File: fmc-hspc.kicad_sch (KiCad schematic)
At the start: 36 parts, among them J12 ASP-184329-01_mounting_holes_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

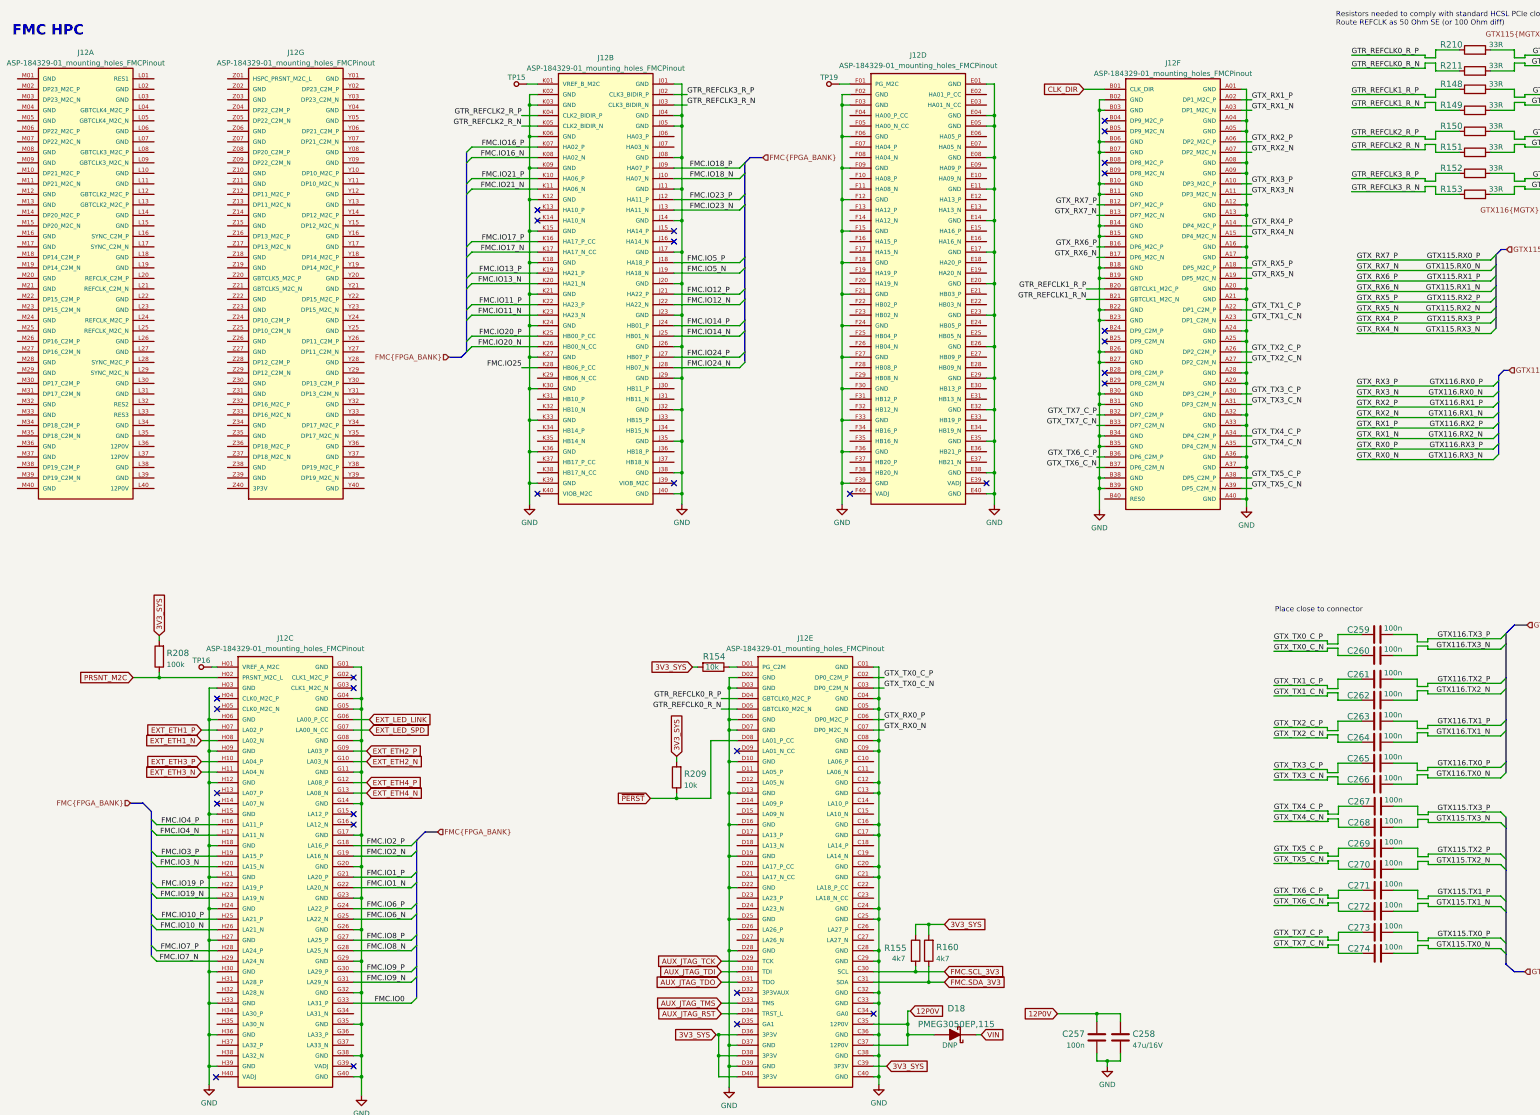
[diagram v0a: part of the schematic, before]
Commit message: Re-annotate the schematic. Export changes to PCB
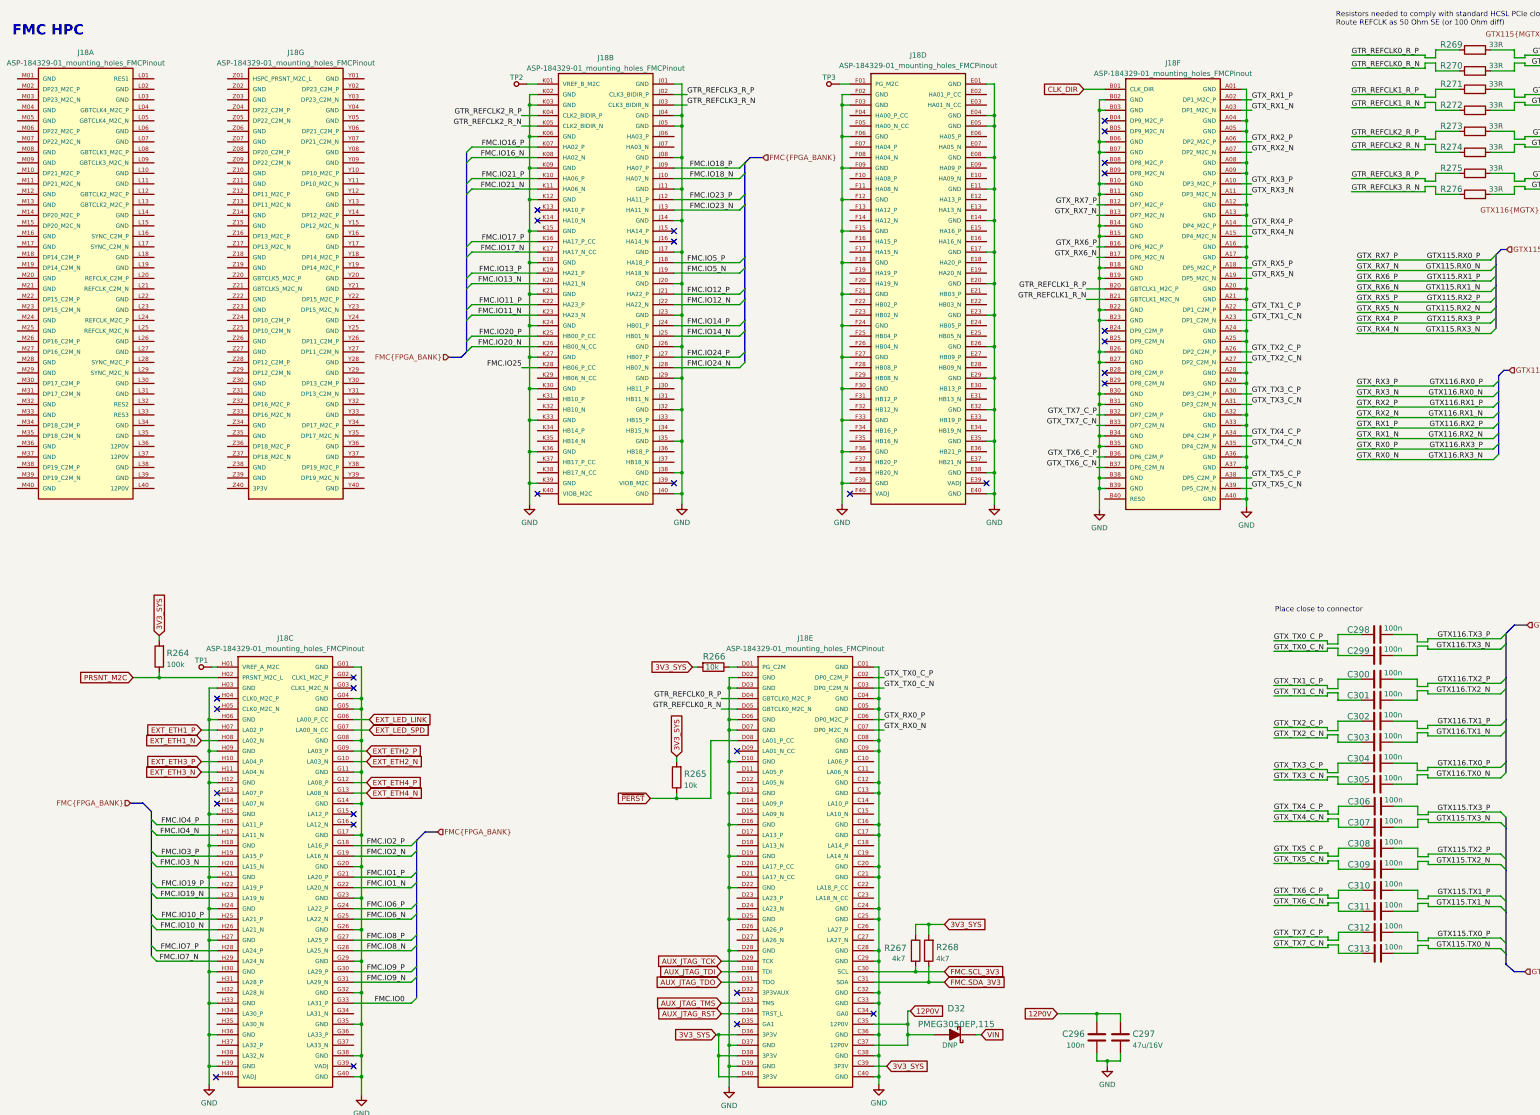
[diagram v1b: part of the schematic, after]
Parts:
- renumbered C257 to C296, C258 to C297, C259 to C298, C260 to C299, C261 to C300, C262 to C301, C263 to C302, C264 to C303, C265 to C304, C266 to C305, C267 to C306, C268 to C307, C269 to C308, C270 to C309, C271 to C310, C272 to C311, C273 to C312, C274 to C313, D18 to D32, J12 to J18, R208 to R264, R209 to R265, R154 to R266, R155 to R267, R160 to R268, R210 to R269, R211 to R270, R148 to R271, R149 to R272, R150 to R273, R151 to R274, R152 to R275, R153 to R276, TP16 to TP1, TP15 to TP2, TP19 to TP3

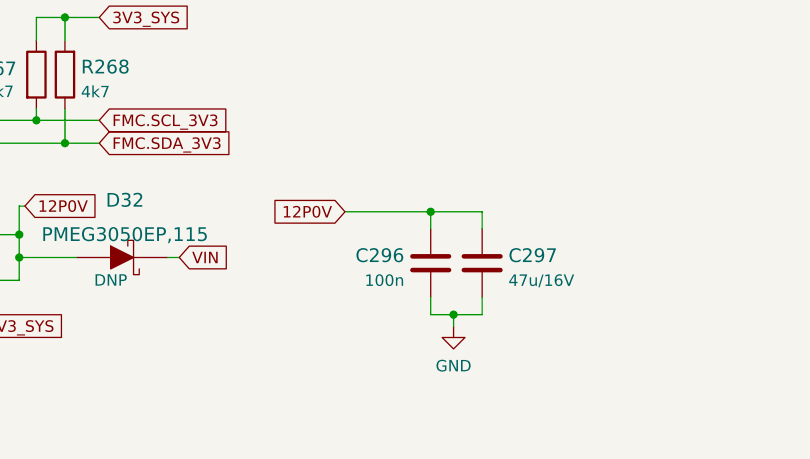
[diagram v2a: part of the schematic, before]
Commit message: Replace 100n to 0402
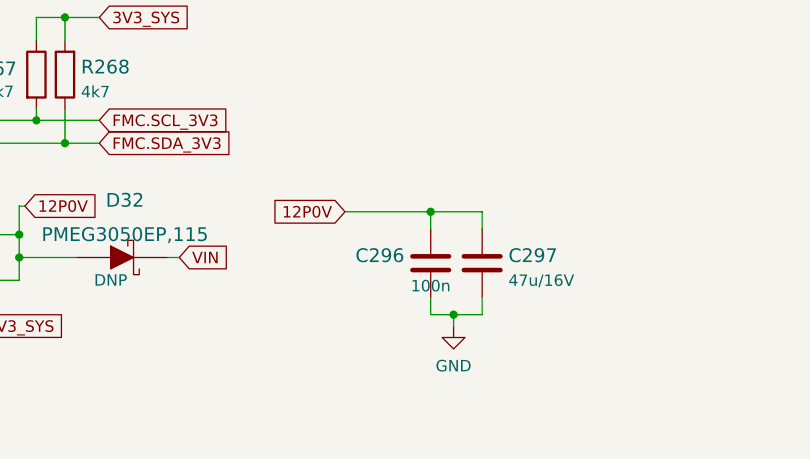
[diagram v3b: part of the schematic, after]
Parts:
- C296: value C_100n_0201 -> C_100n_0402_EIA; footprint antmicro-footprints:0201-res -> antmicro-footprints:0402-cap_EIA; symbol antmicroCapacitorsmisc:C_100n_0201 -> antmicroCapacitors0402:C_100n_0402_EIA; MPN CC0201KRX6S5BB104 -> GRM155R61H104KE14D; Manufacturer YAGEO -> Murata
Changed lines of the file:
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@@
     (pin "2")
   )
-  (symbol (lib_id "antmicroCapacitorsmisc:C_100n_0201") (at 280.035 262.255 0) (unit 1)
+  (symbol (lib_id "antmicroCapacitors0402:C_100n_0402_EIA") (at 280.035 262.255 0) (unit 1)
     (in_bom yes) (on_board yes) (fields_autoplaced)
     (property "Reference" "C296" (id 0) (at 277.114 261.4204 0)
       (effects (font (size 1.524 1.524)) (justify right))
     )
-    (property "Value" "C_100n_0201" (id 1) (at 280.035 266.065 0)
+    (property "Value" "C_100n_0402_EIA" (id 1) (at 280.035 266.065 0)
       (effects (font (size 1.524 1.524)) hide)
     )
-    (property "Footprint" "antmicro-footprints:0201-res" (id 2) (at 285.115 257.175 0)
+    (property "Footprint" "antmicro-footprints:0402-cap_EIA" (id 2) (at 285.115 257.175 0)
       (effects (font (size 1.524 1.524)) (justify left) hide)
     )
@@
       (effects (font (size 1.27 1.27)) hide)
     )
-    (property "Manufacturer" "YAGEO" (id 4) (at 285.115 252.095 0)
+    (property "Manufacturer" "Murata" (id 4) (at 285.115 252.095 0)
       (effects (font (size 1.524 1.524)) (justify left) hide)
     )
-    (property "MPN" "CC0201KRX6S5BB104" (id 5) (at 285.115 254.635 0)
+    (property "MPN" "GRM155R61H104KE14D" (id 5) (at 285.115 254.635 0)
       (effects (font (size 1.524 1.524)) (justify left) hide)
     )
-    (property "Val" "100n" (id 6) (at 277.114 264.1855 0)
-      (effects (font (size 1.27 1.27)) (justify right))
-    )
+    (property "Val" "100n" (id 6) (at 280.035 264.795 0))
     (pin "1")
     (pin "2")

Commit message: Add connection for MGT bank 117 and 118 to FMC+
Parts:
- added C399, C400, C401, C402, C403, C404, C405, C406, C407, C408, C409, C410, C411, C412, C413, C414: C_100n_0402, antmicro-footprints:0402-cap, symbol antmicroCapacitors0402:C_100n_0402
- added R353, R354, R355, R356, R357, R358, R359, R360: R_33R_0402, antmicro-footprints:0402-res, symbol antmicroResistors0402:R_33R_0402
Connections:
- net GND: now also J18.M01 (GND), J18.M04 (GND), J18.M05 (GND), J18.M08 (GND), J18.M09 (GND), J18.M12 (GND), J18.M13 (GND), J18.M16 (GND), J18.M17 (GND), J18.M20 (GND), J18.M21 (GND), J18.M24 (GND), J18.M25 (GND), J18.M28 (GND), J18.M29 (GND), J18.M32 (GND), J18.M33 (GND), J18.M36 (GND), J18.M37 (GND), J18.M40 (GND)
- net at J18.Y01 (GND): now also J18.Y04 (GND), J18.Y05 (GND), J18.Y08 (GND), J18.Y09 (GND), J18.Y12 (GND), J18.Y13 (GND), J18.Y16 (GND), J18.Y17 (GND), J18.Y20 (GND), J18.Y21 (GND), J18.Y24 (GND), J18.Y25 (GND), J18.Y28 (GND), J18.Y29 (GND), J18.Y32 (GND), J18.Y33 (GND), J18.Y36 (GND), J18.Y37 (GND), J18.Y40 (GND)
- net GTX118.RX3_P: now reaches J18.Y10 (DP10_M2C_P)
- net GTX118.RX3_N: now reaches J18.Y11 (DP10_M2C_N)
- net GTX118.RX1_P: now reaches J18.Y14 (DP12_M2C_P)
- net GTX118.RX1_N: now reaches J18.Y15 (DP12_M2C_N)
- net GTX117.RX3_P: now reaches J18.Y18 (DP14_M2C_P)
- net GTX117.RX3_N: now reaches J18.Y19 (DP14_M2C_P)
- net GTX117.RX2_P: now reaches J18.Y22 (DP15_M2C_P)
- net GTX117.RX2_N: now reaches J18.Y23 (DP15_M2C_N)
- net GTX_TX9_C_P: now reaches J18.Y26 (DP11_C2M_P)
- net GTX_TX9_C_P: now also C401.1
- net GTX_TX9_C_N: now reaches J18.Y27 (DP11_C2M_N)
- net GTX_TX9_C_N: now also C402.1
- net GTX_TX11_C_P: now reaches J18.Y30 (DP13_C2M_P)
- net GTX_TX11_C_P: now also C405.1
- net GTX_TX11_C_N: now reaches J18.Y31 (DP13_C2M_N)
- net GTX_TX11_C_N: now also C406.1
- net GTX117.RX0_P: now reaches J18.Y34 (DP17_M2C_P)
- net GTX117.RX0_N: now reaches J18.Y35 (DP17_M2C_N)
- net GTX117.RX1_N: now reaches J18.Z02 (GND)
- net GTX117.RX1_N: now also J18.Z03 (GND), J18.Z06 (GND), J18.Z07 (GND), J18.Z10 (GND), J18.Z11 (GND), J18.Z12 (DP11_M2C_P), J18.Z13 (DP11_M2C_N), J18.Z14 (GND), J18.Z15 (GND), J18.Z16 (DP13_M2C_P), J18.Z17 (DP13_M2C_N), J18.Z18 (GND), J18.Z19 (GND), J18.Z22 (GND), J18.Z23 (GND), J18.Z24 (DP10_C2M_P), J18.Z25 (DP10_C2M_N), J18.Z26 (GND), J18.Z27 (GND), J18.Z28 (DP12_C2M_P), J18.Z29 (DP12_C2M_N), J18.Z30 (GND), J18.Z31 (GND), J18.Z32 (DP16_M2C_P), J18.Z33 (DP16_M2C_N), J18.Z34 (GND), J18.Z35 (GND), J18.Z38 (GND), J18.Z39 (GND), C399.1, C400.1, C403.1, C404.1
- net at J18.L02 (GND): now also J18.L03 (GND), J18.L06 (GND), J18.L07 (GND), J18.L10 (GND), J18.L11 (GND), J18.L14 (GND), J18.L15 (GND), J18.L18 (GND), J18.L19 (GND), J18.L22 (GND), J18.L23 (GND), J18.L26 (GND), J18.L27 (GND), J18.L30 (GND), J18.L31 (GND), J18.L34 (GND), J18.L35 (GND), J18.L38 (GND), J18.L39 (GND)
- net GTX_TX12_C_P: now reaches J18.M18 (DP14_C2M_P)
- net GTX_TX12_C_P: now also C407.1
- net GTX_TX12_C_N: now reaches J18.M19 (DP14_C2M_N)
- net GTX_TX12_C_N: now also C408.1
- net GTX_TX13_C_P: now reaches J18.M22 (DP15_C2M_P)
- net GTX_TX13_C_P: now also C409.1
- net GTX_TX13_C_N: now reaches J18.M23 (DP15_C2M_N)
- net GTX_TX13_C_N: now also C410.1
- net GTX_TX14_C_P: now reaches J18.M26 (DP16_C2M_P)
- net GTX_TX14_C_P: now also C411.1
- net GTX_TX14_C_N: now reaches J18.M27 (DP16_C2M_N)
- net GTX_TX14_C_N: now also C412.1
- net GTX_TX15_C_P: now reaches J18.M30 (DP17_C2M_P)
- net GTX_TX15_C_P: now also C413.1
- net GTX_TX15_C_N: now reaches J18.M31 (DP17_C2M_N)
- net GTX_TX15_C_N: now also C414.1
- new net GTR_REFCLK4_R_N: R354.1
- new net GTR_REFCLK4_R_P: R353.1
- new net GTR_REFCLK5_R_N: R356.1
- new net GTR_REFCLK5_R_P: R355.1
- new net GTR_REFCLK6_R_N: R358.1
- new net GTR_REFCLK6_R_P: R357.1
- new net GTR_REFCLK7_R_N: R360.1
- new net GTR_REFCLK7_R_P: R359.1
- new net GTX117.REFCLK0_N: R354.2
- new net GTX117.REFCLK0_P: R353.2
- new net GTX117.REFCLK1_N: R356.2
- new net GTX117.REFCLK1_P: R355.2
- new net GTX117.TX0_N: C414.2
- new net GTX117.TX0_P: C413.2
- new net GTX117.TX1_N: C412.2
- new net GTX117.TX1_P: C411.2
- new net GTX117.TX2_N: C410.2
- new net GTX117.TX2_P: C409.2
- new net GTX117.TX3_N: C408.2
- new net GTX117.TX3_P: C407.2
- new net GTX118.REFCLK0_N: R358.2
- new net GTX118.REFCLK0_P: R357.2
- new net GTX118.REFCLK1_N: R360.2
- new net GTX118.REFCLK1_P: R359.2
- new net GTX118.TX0_N: C406.2
- new net GTX118.TX0_P: C405.2
- new net GTX118.TX1_N: C404.2
- new net GTX118.TX1_P: C403.2
- new net GTX118.TX2_N: C402.2
- new net GTX118.TX2_P: C401.2
- new net GTX118.TX3_N: C400.2
- new net GTX118.TX3_P: C399.2
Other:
- moved on the sheet: C296, C297, C298, C299, C300, C301, C302, C303, C304, C305, C306, C307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

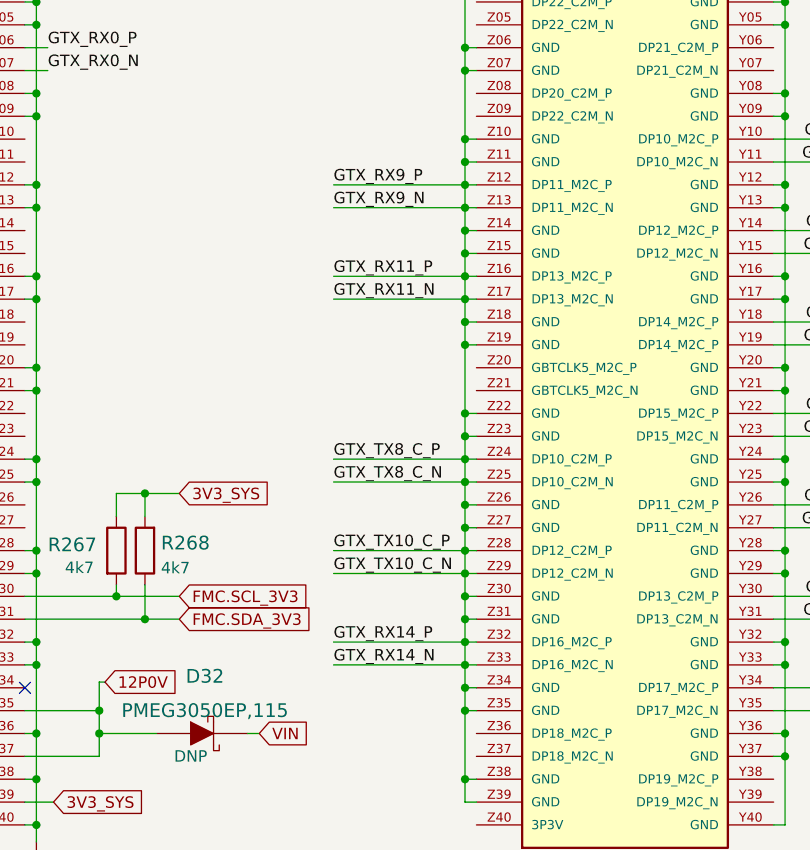
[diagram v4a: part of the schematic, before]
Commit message: Dix GTX signals connected to GND
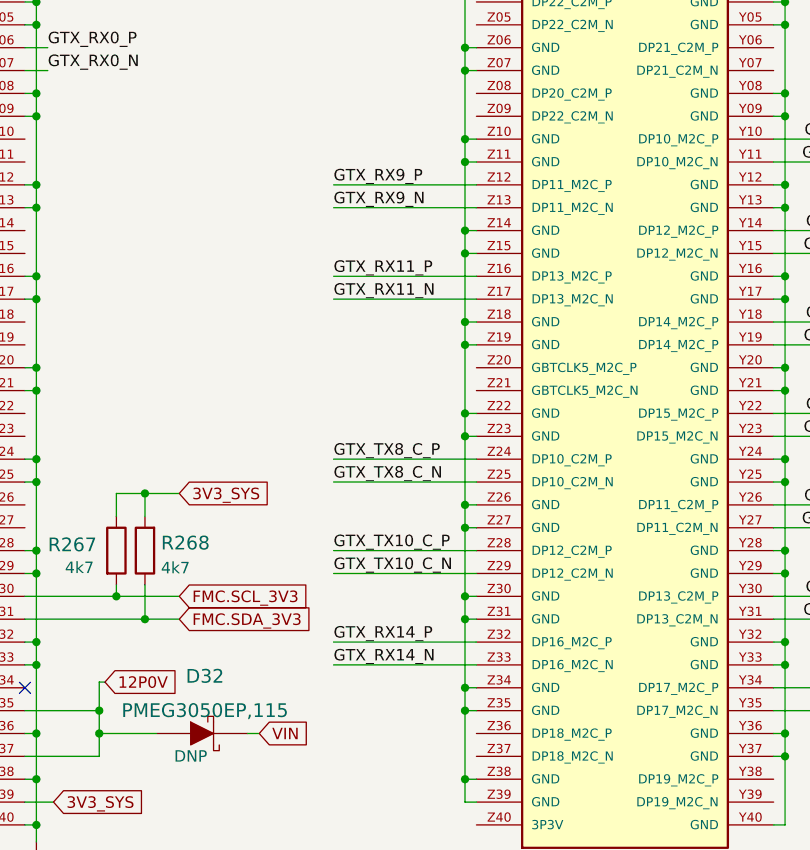
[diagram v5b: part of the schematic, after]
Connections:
- net GTX117.RX1_N: no longer C399.1, C400.1, C403.1, C404.1, J18.Z02 (GND), J18.Z03 (GND), J18.Z06 (GND), J18.Z07 (GND), J18.Z10 (GND), J18.Z11 (GND), J18.Z12 (DP11_M2C_P), J18.Z13 (DP11_M2C_N), J18.Z14 (GND), J18.Z15 (GND), J18.Z16 (DP13_M2C_P), J18.Z17 (DP13_M2C_N), J18.Z18 (GND), J18.Z19 (GND), J18.Z22 (GND), J18.Z23 (GND), J18.Z24 (DP10_C2M_P), J18.Z25 (DP10_C2M_N), J18.Z26 (GND), J18.Z27 (GND), J18.Z28 (DP12_C2M_P), J18.Z29 (DP12_C2M_N), J18.Z30 (GND), J18.Z31 (GND), J18.Z32 (DP16_M2C_P), J18.Z34 (GND), J18.Z35 (GND), J18.Z38 (GND), J18.Z39 (GND)
- new net: J18.Z02 (GND), J18.Z03 (GND), J18.Z06 (GND), J18.Z07 (GND), J18.Z10 (GND), J18.Z11 (GND), J18.Z14 (GND), J18.Z15 (GND), J18.Z18 (GND), J18.Z19 (GND), J18.Z22 (GND), J18.Z23 (GND), J18.Z26 (GND), J18.Z27 (GND), J18.Z30 (GND), J18.Z31 (GND), J18.Z34 (GND), J18.Z35 (GND), J18.Z38 (GND), J18.Z39 (GND)
- new net GTX117.RX1_P: J18.Z32 (DP16_M2C_P)
- new net GTX118.RX0_N: J18.Z17 (DP13_M2C_N)
- new net GTX118.RX0_P: J18.Z16 (DP13_M2C_P)
- new net GTX118.RX2_N: J18.Z13 (DP11_M2C_N)
- new net GTX118.RX2_P: J18.Z12 (DP11_M2C_P)
- new net GTX_TX10_C_N: C404.1, J18.Z29 (DP12_C2M_N)
- new net GTX_TX10_C_P: C403.1, J18.Z28 (DP12_C2M_P)
- new net GTX_TX8_C_N: C400.1, J18.Z25 (DP10_C2M_N)
- new net GTX_TX8_C_P: C399.1, J18.Z24 (DP10_C2M_P)

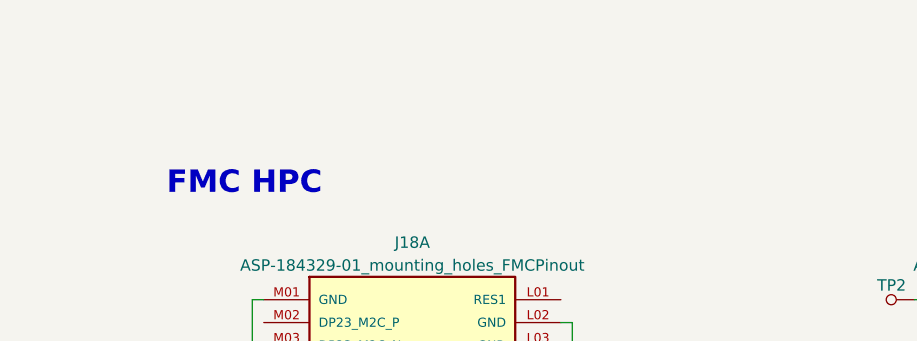
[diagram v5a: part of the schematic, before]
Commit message: Add FMC+ to do's
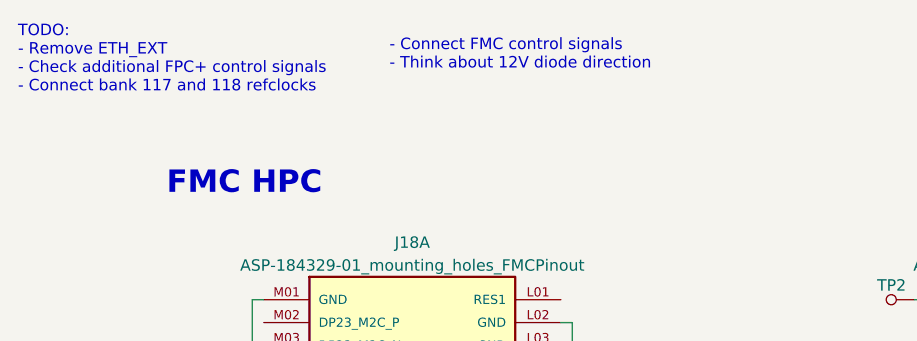
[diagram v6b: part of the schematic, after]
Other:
- note added: "- Connect FMC control signals - Think about 12V diode direction"
- note added: "TODO: - Remove ETH_EXT - Check additional FPC+ control signals - Connect bank 117 and 118 refclocks"
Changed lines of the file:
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@@
+    (effects (font (size 1.27 1.27)) (justify left bottom))
+  )
+  (text "TODO:\n- Remove ETH_EXT\n- Check additional FPC+ control signals\n- Connect bank 117 and 118 refclocks\n"
+    (at 1.27 8.89 0)
     (effects (font (size 1.27 1.27)) (justify left bottom))
   )
@@
     (effects (font (size 1.27 1.27)) (justify left bottom))
   )
+  (text "- Connect FMC control signals\n- Think about 12V diode direction "
+    (at 42.545 6.35 0)
+    (effects (font (size 1.27 1.27)) (justify left bottom))
+  )
